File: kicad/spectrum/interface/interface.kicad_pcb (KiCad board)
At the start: 2 copper layers, 99.1 x 99.1 mm, 23 parts, among them J1 H-MS1110_Bus, J2 EXT_INPUT, J3 SYNC, J4 ROT, J5 CONTROL, J6 FP_POWER, J7 SPECT, J8 I2C, U1 MP1584EN_module, U2 L78L12_TO92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

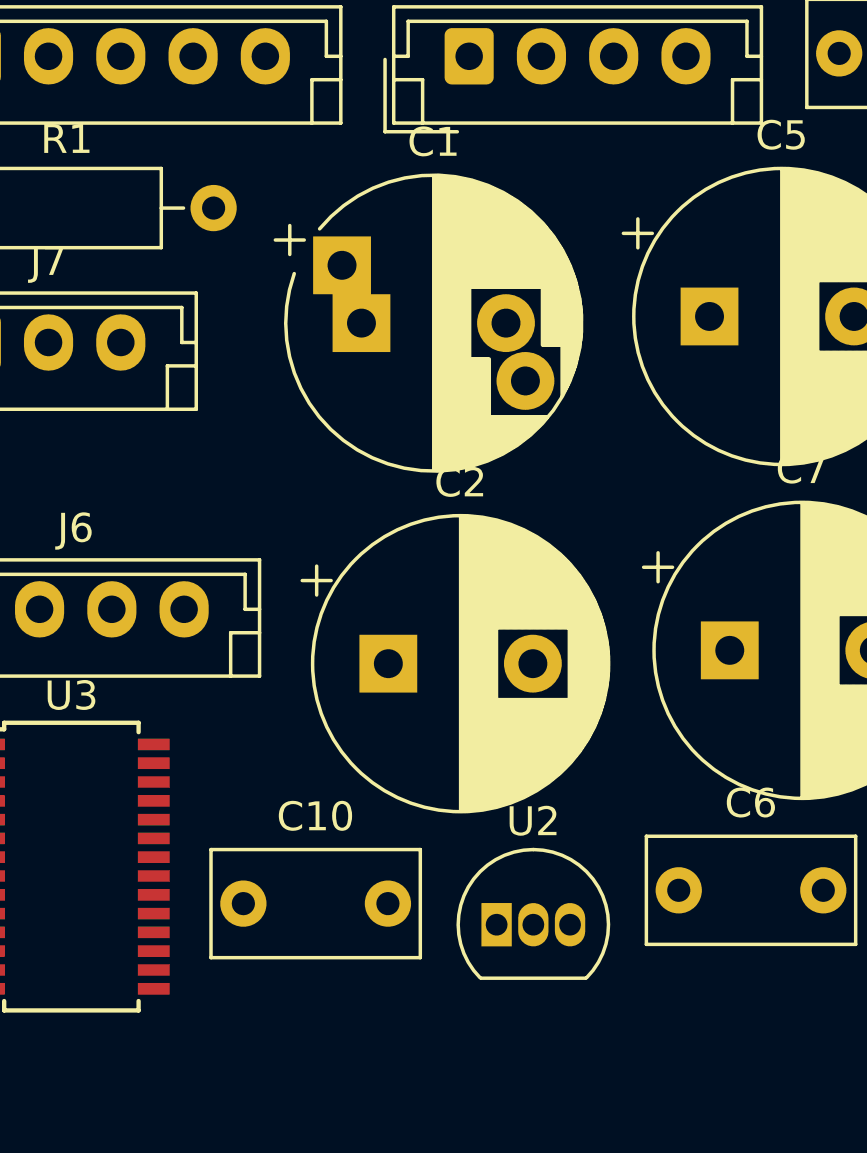
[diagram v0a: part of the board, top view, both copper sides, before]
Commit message: Update spectrum interface to Kicad 7
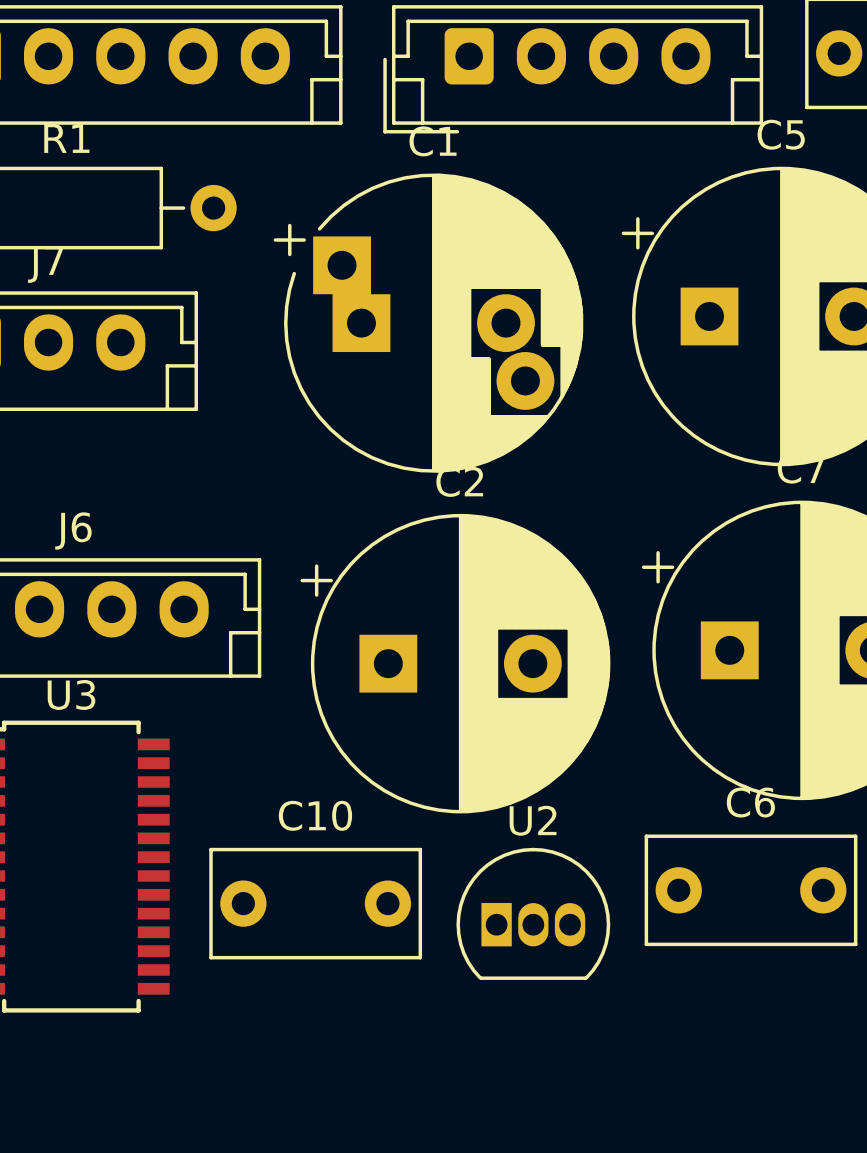
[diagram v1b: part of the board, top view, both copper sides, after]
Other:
- net class Default removed
